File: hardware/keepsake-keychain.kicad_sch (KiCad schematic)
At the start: 44 parts, among them Q1 MMFTP4042K, Q2 MMFTP4042K, Q3 MMFTP4042K, Q4 MMFTP4042K, SW1 SPDT Power Switch, SW2 R-667842, U1 ATTINY1614, U2 74HC595 RED Shift Register, U3 74HC595 GREEN Shift Register, U4 74HC595 BLUE Shift Register

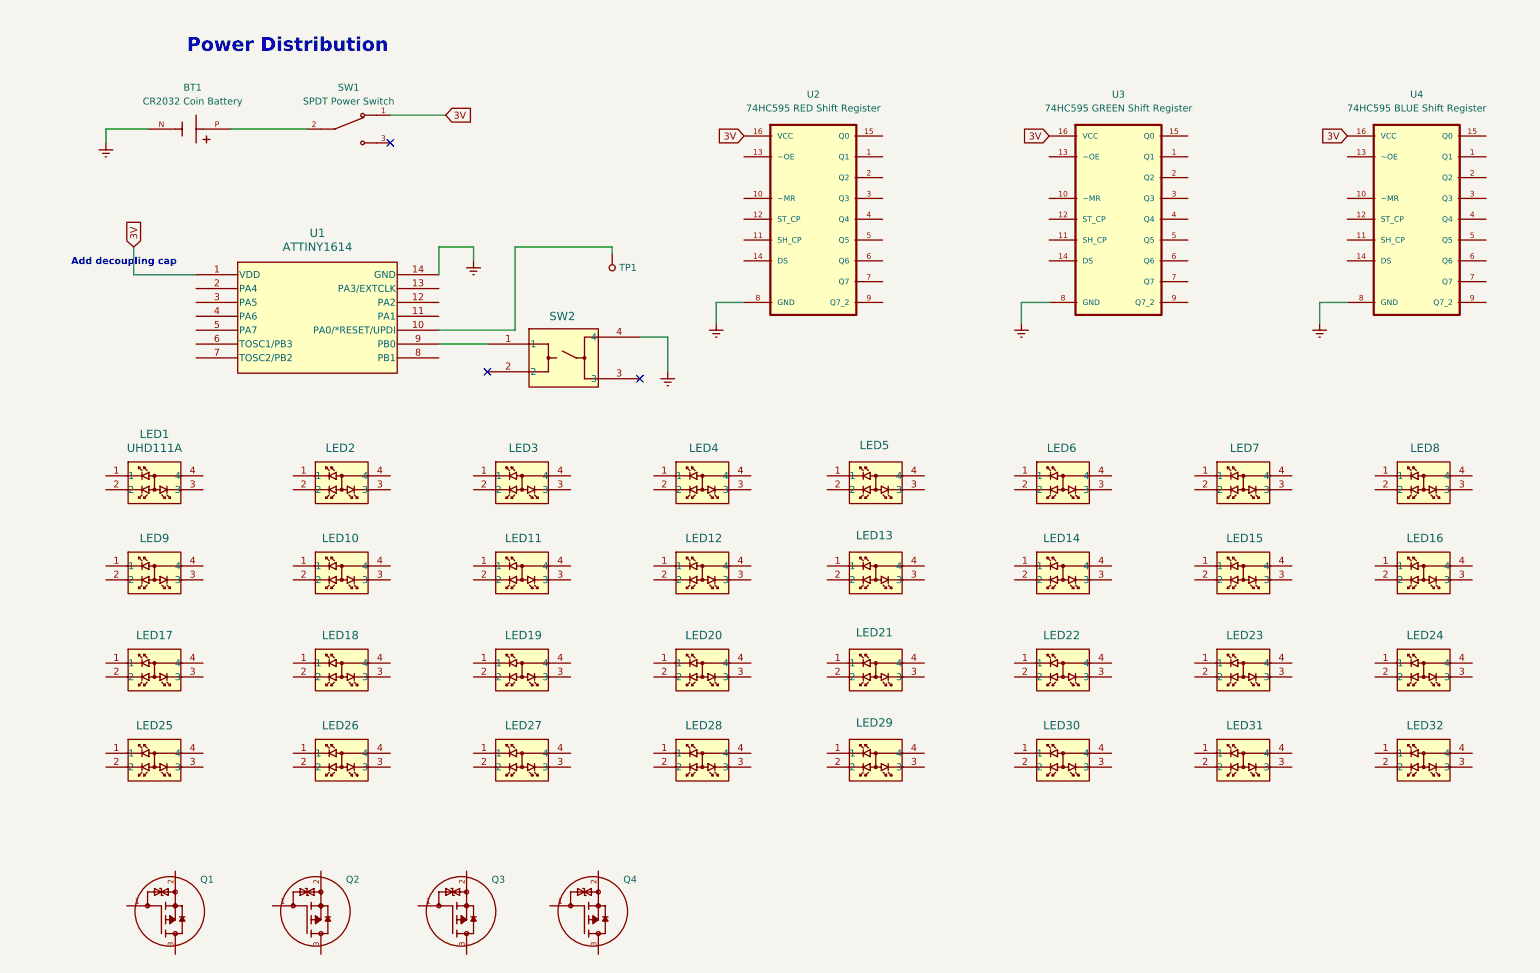
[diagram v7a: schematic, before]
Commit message: Connect MOSFETs, add MEMS microphone
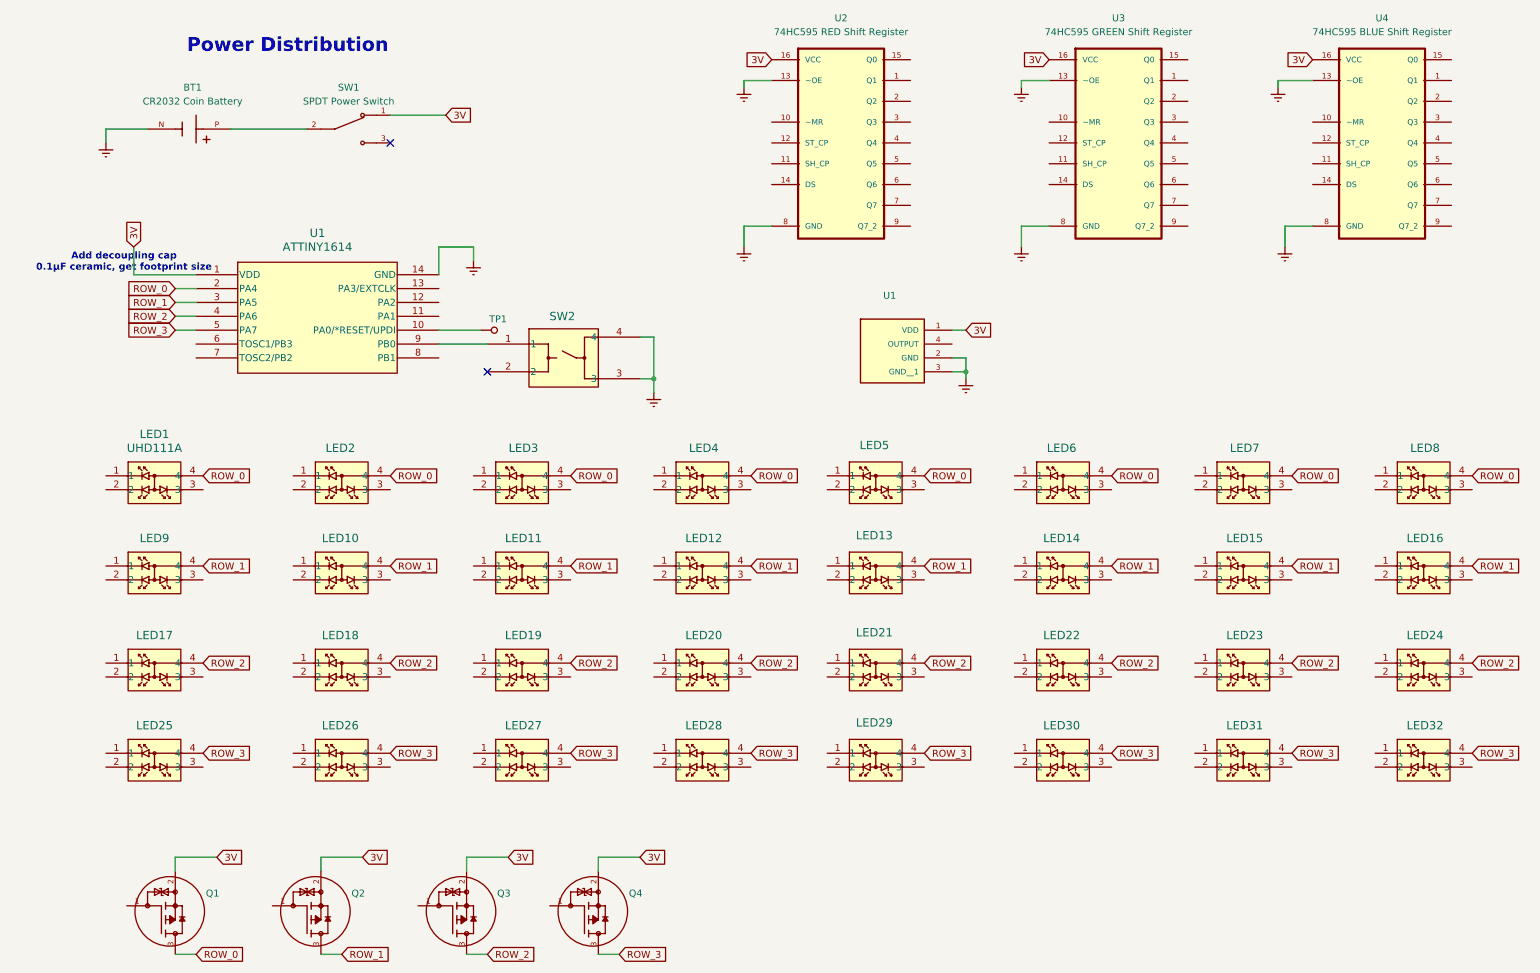
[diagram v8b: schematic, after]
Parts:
- added U1: 3SM123C4T1QA, 3SM123C4T1QA:MIC_3SM123C4T1QA, symbol 0_MEMS_Microphone:3SM123C4T1QA
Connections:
- net 3V: now also Q1.2, Q2.2, Q3.2, Q4.2, U1.1 (VDD)
- net GND: now also SW2.3, U2.13 (~OE), U3.13 (~OE), U4.13 (~OE), U1.2 (GND), U1.3 (GND__1)
- net ROW_0: now reaches U1.2 (PA4)
- net ROW_0: now also LED1.4, LED2.4, LED3.4, LED4.4, LED5.4, LED6.4, LED7.4, LED8.4, Q1.3
- net ROW_1: now reaches U1.3 (PA5)
- net ROW_1: now also LED10.4, LED11.4, LED12.4, LED13.4, LED14.4, LED15.4, LED16.4, LED9.4, Q2.3
- net ROW_2: now reaches U1.4 (PA6)
- net ROW_2: now also LED17.4, LED18.4, LED19.4, LED20.4, LED21.4, LED22.4, LED23.4, LED24.4, Q3.3
- net ROW_3: now reaches U1.5 (PA7)
- net ROW_3: now also LED25.4, LED26.4, LED27.4, LED28.4, LED29.4, LED30.4, LED31.4, LED32.4, Q4.3
- no-connect marks 3 -> 2
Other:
- note added: "Add decoupling cap 0.1µF ceramic, get footprint size"
- note removed: "Add decoupling cap"
- moved on the sheet: TP1, U2, U3, U4
